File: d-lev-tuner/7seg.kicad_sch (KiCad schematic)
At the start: 8 parts

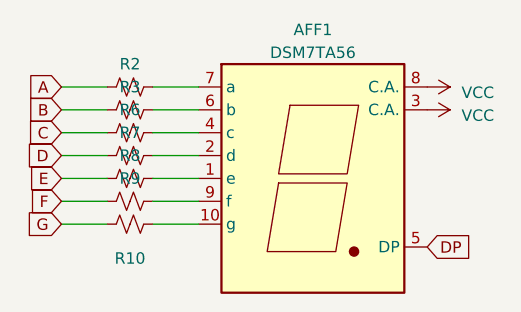
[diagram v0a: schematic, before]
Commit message: finished routing tuner
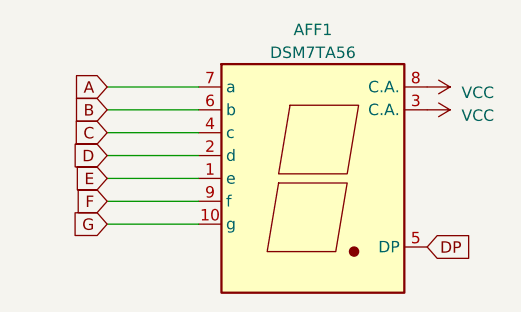
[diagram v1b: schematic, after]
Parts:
- removed R10, R2, R3, R6, R7, R8, R9: R_Small_US, Resistor_SMD:R_0603_1608Metric, symbol Device:R_Small_US
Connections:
- net A: now also AFF1.7 (a)
- net B: now also AFF1.6 (b)
- net C: now also AFF1.4 (c)
- net D: now also AFF1.2 (d)
- net E: now also AFF1.1 (e)
- net F: now also AFF1.9 (f)
- net G: now also AFF1.10 (g)

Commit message: Add iBOMs and additional part numbers
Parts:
- AFF1: MPN (none) -> 593-DSM7TA56106T; Supplier (none) -> Mouser; Supplier URL (none) -> https://www.mouser.com/ProductDetail/593-DSM7TA56106T
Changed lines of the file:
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@@
+      (effects (font (size 1.27 1.27)) hide)
+    )
+    (property "MPN" "593-DSM7TA56106T" (at 129.54 105.41 0)
+      (effects (font (size 1.27 1.27)) hide)
+    )
+    (property "Supplier" "Mouser" (at 129.54 105.41 0)
+      (effects (font (size 1.27 1.27)) hide)
+    )
+    (property "Supplier URL" "https://www.mouser.com/ProductDetail/593-DSM7TA56106T" (at 129.54 105.41 0)
+      (effects (font (size 1.27 1.27)) hide)
+    )
+    (property "Notes" "" (at 129.54 105.41 0)
+      (effects (font (size 1.27 1.27)) hide)
+    )
+    (property "Supplier Alt" "" (at 129.54 105.41 0)
+      (effects (font (size 1.27 1.27)) hide)
+    )
+    (property "Supplier Alt URL" "" (at 129.54 105.41 0)
       (effects (font (size 1.27 1.27)) hide)
     )
